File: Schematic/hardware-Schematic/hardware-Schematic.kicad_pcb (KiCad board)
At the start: 2 copper layers, 23 parts, among them J1 DC 5V Input, J2 12 PIN IDC, J3 speaker, Q1 NDP6020P, SW1 top, SW2 reset, SW3 load, U1 ATmega328P-P, U14 YP-05, U15 SN74AHCT125N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

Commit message: started the rooting but some thing moved and now every thing is miss placed I must start from the beginning again
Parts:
- C1, C2: footprint Capacitor_THT:C_Rect_L7.2mm_W3.0mm_P5.00mm_FKS2_FKP2_MKS2_MKP2 -> Capacitor_THT:C_Axial_L12.0mm_D6.5mm_P15.00mm_Horizontal
- moved J3 37.2 mm to (219.2, 112.7), turned to 90 degrees
- moved R12 29.6 mm to (209.4, 101.5)
- moved C1 29.3 mm to (116.0, 113.6), turned to 180 degrees
- moved R1 27.0 mm to (84.5, 107.1), turned to 90 degrees
- moved C7 24.7 mm to (65.5, 112.8), turned to -90 degrees
- moved J2 24.1 mm to (150.0, 82.5)
- moved SW2 23.2 mm to (85.8, 111.8)
- moved R13 22.9 mm to (209.4, 98.5)
- moved C3 22.6 mm to (102.5, 86.5)
- moved Q1 22.4 mm to (217.5, 89.5), turned to 180 degrees
- moved C2 22.4 mm to (116.0, 93.1), turned to 180 degrees
- moved U1 22.2 mm to (90.8, 107.1)
- moved U15 21.3 mm to (185.8, 103.0), turned to 90 degrees
- moved R11 19.4 mm to (172.7, 83.2)
- moved U3 19.2 mm to (143.3, 103.0)
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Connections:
- U17 pad 5: +3.3V -> GND
- U17 pad 8: GND -> +3.3V
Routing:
- net GND: track 0.00 -> 287.1 mm
- net +5V: track 0.00 -> 127.6 mm
- net +3.3V: track 0.00 -> 107.0 mm
- net Net-(U1-PD0): track 0.00 -> 71.4 mm
- net Net-(SW2A-D): track 0.00 -> 68.6 mm
- net Net-(U1-PD1): track 0.00 -> 66.3 mm
- net Net-(U1-PD2): track 0.00 -> 56.8 mm
- net Net-(U1-PD4): track 0.00 -> 56.5 mm
- net Net-(U1-PD6): track 0.00 -> 35.1 mm
- net Net-(U1-PC3): track 0.00 -> 26.1 mm
- net Net-(J2-Pad4): track 0.00 -> 25.5 mm
- net Net-(Q1-G): track 0.00 -> 24.0 mm
- net Net-(J2-Pad1): track 0.00 -> 23.0 mm
- net Net-(J2-Pad3): track 0.00 -> 21.8 mm
- net Net-(U1-PC5): track 0.00 -> 19.4 mm
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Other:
- board outline added: 190 x 45 mm

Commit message: Further work on the hardware side of the pcb
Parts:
- moved U3 12.2 mm to (131.4, 100.5)
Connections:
- J2 pad 1: Net-(J2-Pad1) -> Net-(U1-PD7)
- J2 pad 10: +5V -> Net-(J2-Pad10)
- J2 pad 11: +3.3V -> Net-(J2-Pad11)
- J2 pad 2: Net-(J2-Pad2) -> Net-(U1-PD3)
- J2 pad 3: Net-(J2-Pad3) -> Net-(U1-PD6)
- J2 pad 4: Net-(J2-Pad4) -> Net-(U1-PD4)
- J2 pad 5: Net-(U1-PD4) -> Net-(U1-PD2)
- J2 pad 6: Net-(U1-PD7) -> +3.3V
- J2 pad 7: Net-(U1-PD6) -> +5V
- J2 pad 8: Net-(U1-PD2) -> Net-(J2-Pad8)
- J2 pad 9: Net-(U1-PD3) -> Net-(J2-Pad9)
- U1 pad 23: Net-(U1-PC0) -> unconnected-(U1-PC0-Pad23)
- U1 pad 9: unconnected-(U1-XTAL1/PB6-Pad9) -> Net-(U1-XTAL1/PB6)
- U15 pad 12: Net-(U1-PC0) -> Net-(U1-XTAL1/PB6)
- U3 pad 11: Net-(J2-Pad2) -> Net-(J2-Pad11)
- U3 pad 12: Net-(U1-PB4) -> Net-(U1-PB5)
- U3 pad 2: Net-(U1-PB5) -> Net-(U1-PB2)
- U3 pad 3: Net-(J2-Pad3) -> Net-(J2-Pad8)
- U3 pad 6: Net-(J2-Pad1) -> Net-(J2-Pad9)
- U3 pad 8: Net-(J2-Pad4) -> Net-(J2-Pad10)
- U3 pad 9: Net-(U1-PB2) -> Net-(U1-PB4)
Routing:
- net Net-(U1-PB1): track 0.00 -> 155.9 mm
- net Net-(U1-XTAL1/PB6): track 0.00 -> 146.6 mm
- net Net-(U1-PB0): track 0.00 -> 98.0 mm
- net GND: track 287.1 -> 352.0 mm
- net Net-(U1-PD4): track 56.5 -> 23.4 mm
- net Net-(J2-Pad8): track 0.00 -> 31.3 mm
- net Net-(U1-PD6): track 35.1 -> 4.14 mm
- net Net-(U1-PB4): track 0.00 -> 30.6 mm
- net Net-(U1-PD2): track 56.8 -> 27.6 mm
- net Net-(J2-Pad9): track 0.00 -> 26.1 mm
- net Net-(U1-PB5): track 0.00 -> 25.5 mm
- net Net-(J2-Pad4): track 25.5 -> 0.00 mm
- net Net-(U1-PB3): track 0.00 -> 24.9 mm
- net Net-(J2-Pad1): track 23.0 -> 0.00 mm
- net Net-(J2-Pad3): track 21.8 -> 0.00 mm
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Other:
- board size 190 x 45 mm -> 198.5 x 45 mm

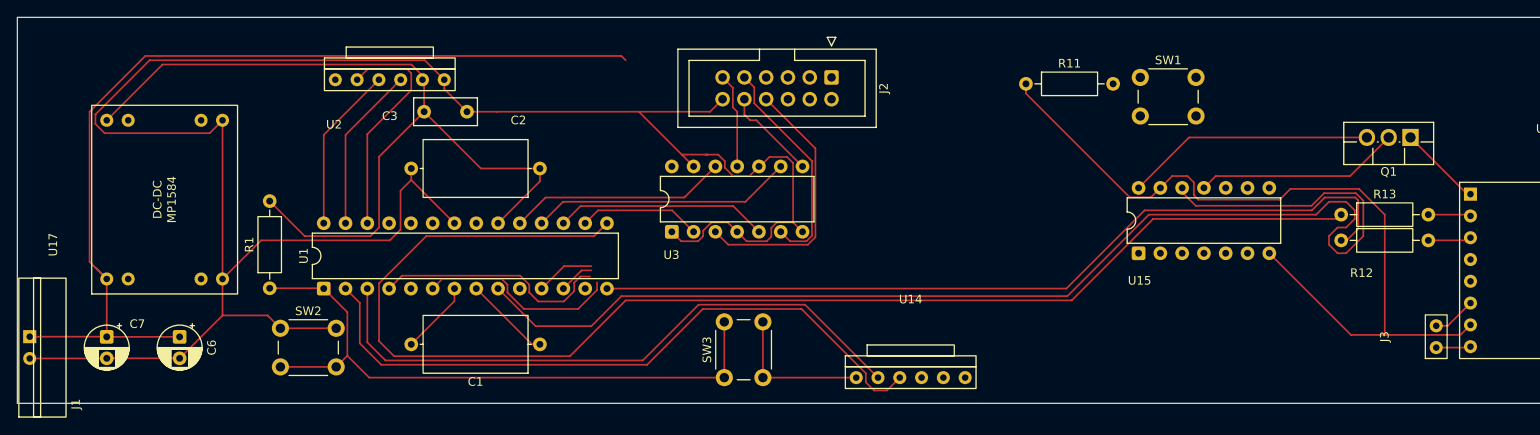
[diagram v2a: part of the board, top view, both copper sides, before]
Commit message: Finished the PCBs. I had to use two jumper cable. I also adjusted the position of some traces close to pins
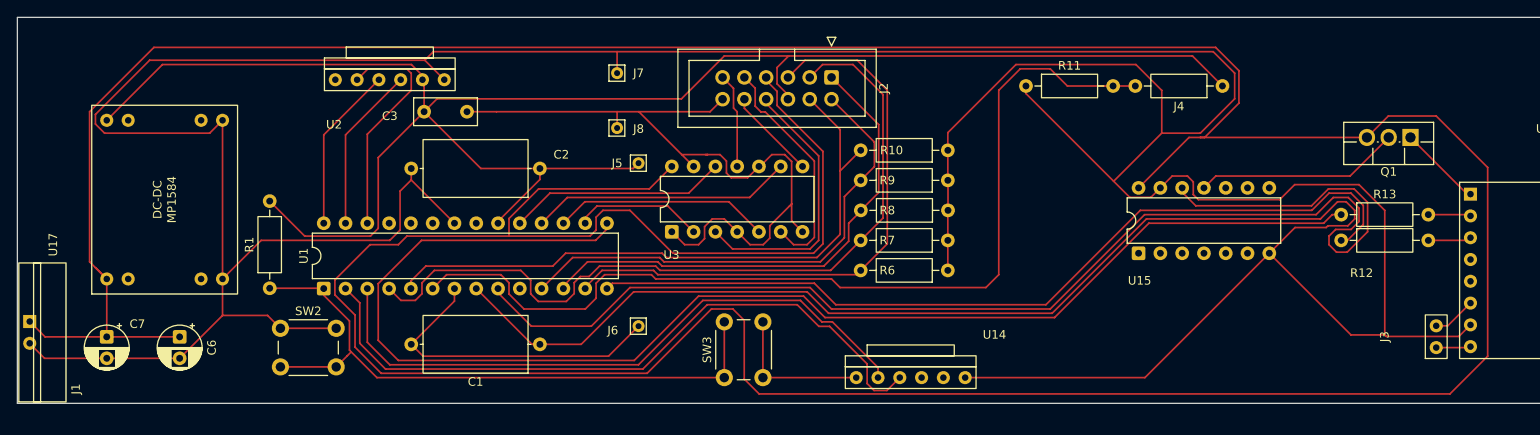
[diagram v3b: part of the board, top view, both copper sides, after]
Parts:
- removed SW1: top, Button_Switch_THT:SW_PUSH_6mm
- added J4: Conn_01x02_Pin, Resistor_THT:R_Axial_DIN0207_L6.3mm_D2.5mm_P10.16mm_Horizontal, F.Cu at (195.6, 83.5)
- added J5: 3.3V Jumper 1, Connector_Pin:Pin_D0.7mm_L6.5mm_W1.8mm_FlatFork, F.Cu at (127.5, 92.5)
- added J6: 3.3V Jumper 2, Connector_Pin:Pin_D0.7mm_L6.5mm_W1.8mm_FlatFork, F.Cu at (127.5, 111.5)
- added J7: GND Jumper 1, Connector_Pin:Pin_D0.7mm_L6.5mm_W1.8mm_FlatFork, F.Cu at (125.0, 82.0)
- added J8: GND Jumper 2, Connector_Pin:Pin_D0.7mm_L6.5mm_W1.8mm_FlatFork, F.Cu at (125.0, 88.4)
- added R10: 10k, Resistor_THT:R_Axial_DIN0207_L6.3mm_D2.5mm_P10.16mm_Horizontal, F.Cu at (163.6, 91.0)
- added R6: 10k, Resistor_THT:R_Axial_DIN0207_L6.3mm_D2.5mm_P10.16mm_Horizontal, F.Cu at (163.6, 105.0)
- added R7: 10k, Resistor_THT:R_Axial_DIN0207_L6.3mm_D2.5mm_P10.16mm_Horizontal, F.Cu at (163.6, 101.5)
- added R8: 10k, Resistor_THT:R_Axial_DIN0207_L6.3mm_D2.5mm_P10.16mm_Horizontal, F.Cu at (163.6, 98.0)
- added R9: 10k, Resistor_THT:R_Axial_DIN0207_L6.3mm_D2.5mm_P10.16mm_Horizontal, F.Cu at (163.6, 94.5)
- moved J1 1.77 mm to (55.2, 112.2)
- moved R11 0.25 mm to (172.7, 83.5)
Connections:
- J2 pad 1: Net-(U1-PD7) -> Net-(U1-PD6)
- J2 pad 2: Net-(U1-PD3) -> Net-(U1-PD5)
- J2 pad 3: Net-(U1-PD6) -> Net-(U1-PD2)
- J2 pad 4: Net-(U1-PD4) -> Net-(U1-PD3)
- J2 pad 5: Net-(U1-PD2) -> Net-(U1-PD7)
- R11 pad 2: Net-(SW1A-C) -> Net-(J4-Pin_2)
- U1 pad 11: Net-(SW1A-C) -> Net-(U1-PD5)
- U1 pad 6: Net-(U1-PD4) -> Net-(J4-Pin_2)
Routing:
- net +5V: track 140.9 -> 528.5 mm
- net GND: track 352.0 -> 682.1 mm
- net +3.3V: track 108.1 -> 251.7 mm
- net Net-(J4-Pin_2): track 0.00 -> 112.3 mm
- net Net-(U1-PD3): track 0.00 -> 74.2 mm
- net Net-(U1-PD7): track 0.00 -> 69.6 mm
- net Net-(U1-PD2): track 27.6 -> 93.0 mm
- net Net-(U1-PD5): track 0.00 -> 57.9 mm
- net Net-(U1-PD6): track 4.14 -> 59.0 mm
- net Net-(U1-PD4): track 23.4 -> 0.00 mm
- net Net-(SW1A-C): track 6.89 -> 0.00 mm
- net Net-(U1-XTAL1/PB6): track 146.6 -> 151.6 mm
- net Net-(U1-PB0): track 98.0 -> 101.0 mm
- net Net-(U1-PB1): track 155.9 -> 158.9 mm
- net Net-(U1-PD0): track 78.9 -> 80.5 mm
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
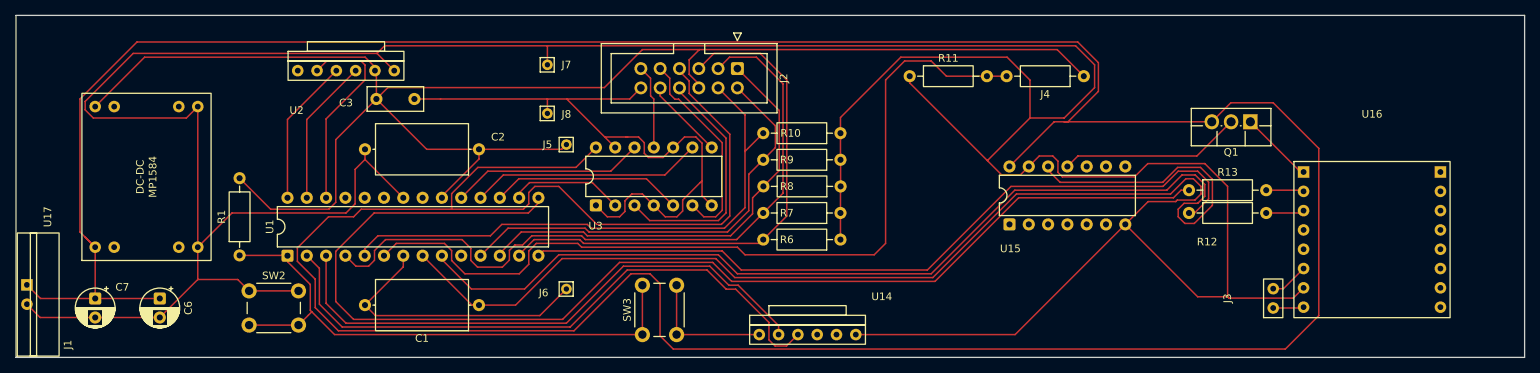
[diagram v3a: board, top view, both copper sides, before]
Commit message: Created gerber  files
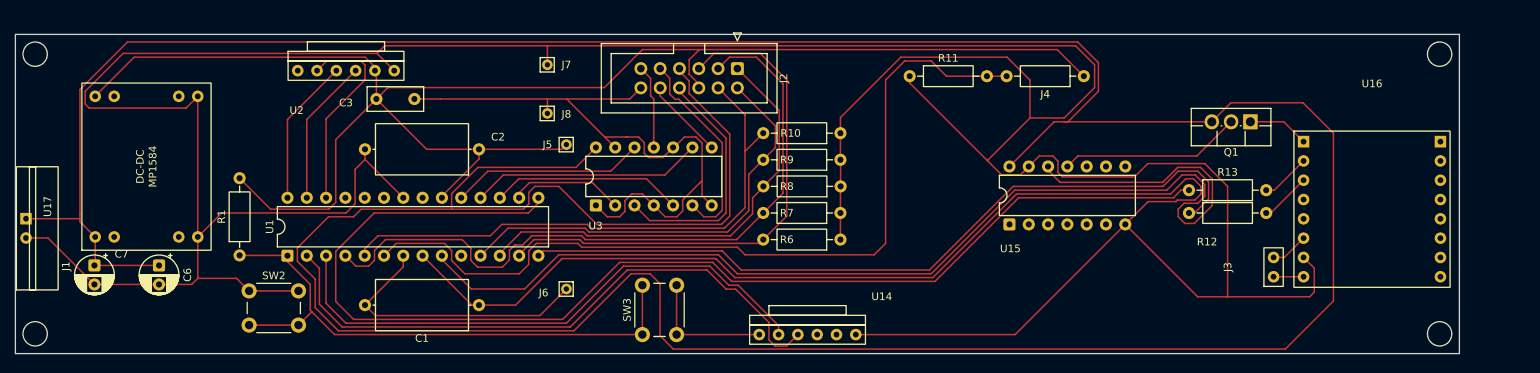
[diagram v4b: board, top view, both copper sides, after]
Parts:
- moved J1 8.71 mm to (55.1, 103.5)
- moved C6 4.35 mm to (73.9, 108.4)
- moved C7 4.35 mm to (65.4, 108.4)
- moved J3 4.11 mm to (219.3, 108.6)
- moved U16 4.00 mm to (233.5, 92.1)
- moved U17 1.35 mm to (63.8, 106.4)
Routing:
- net GND: track 682.1 -> 689.0 mm
- net +5V: track 528.5 -> 524.3 mm
- net Net-(Q1-D): track 9.73 -> 8.08 mm
- net Net-(U16-TX): track 5.04 -> 6.70 mm
- net Net-(U16-RX): track 4.98 -> 6.51 mm
- net +3.3V: track 251.7 -> 251.1 mm
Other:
- board size 198.5 x 45 mm -> 190 x 42 mm
- board text added: "${REFERENCE}"
